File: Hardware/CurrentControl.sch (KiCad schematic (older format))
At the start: 23 parts, among them J4 Screw_Terminal_01x03, Q1 BUK7M45-40EX, U3 DAC121C081CIMK, U4 TLV172IDCK, U5 TLV172IDCK

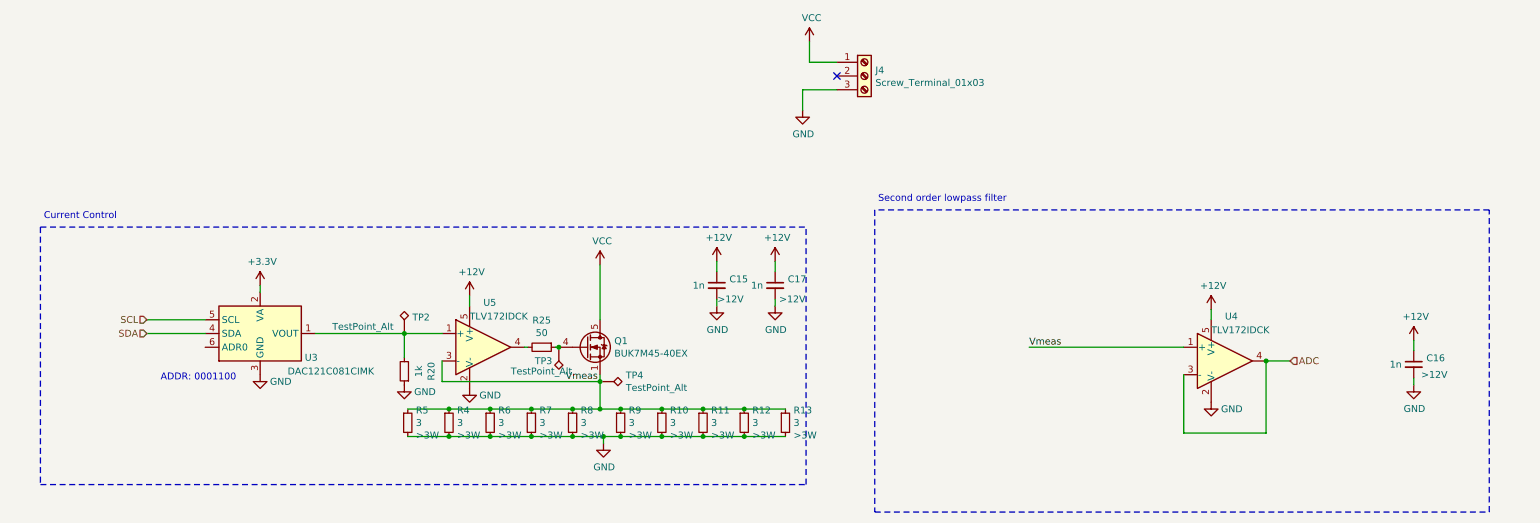
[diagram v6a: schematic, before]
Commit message: Added new FET and opamp. Repositioned parts on PCB
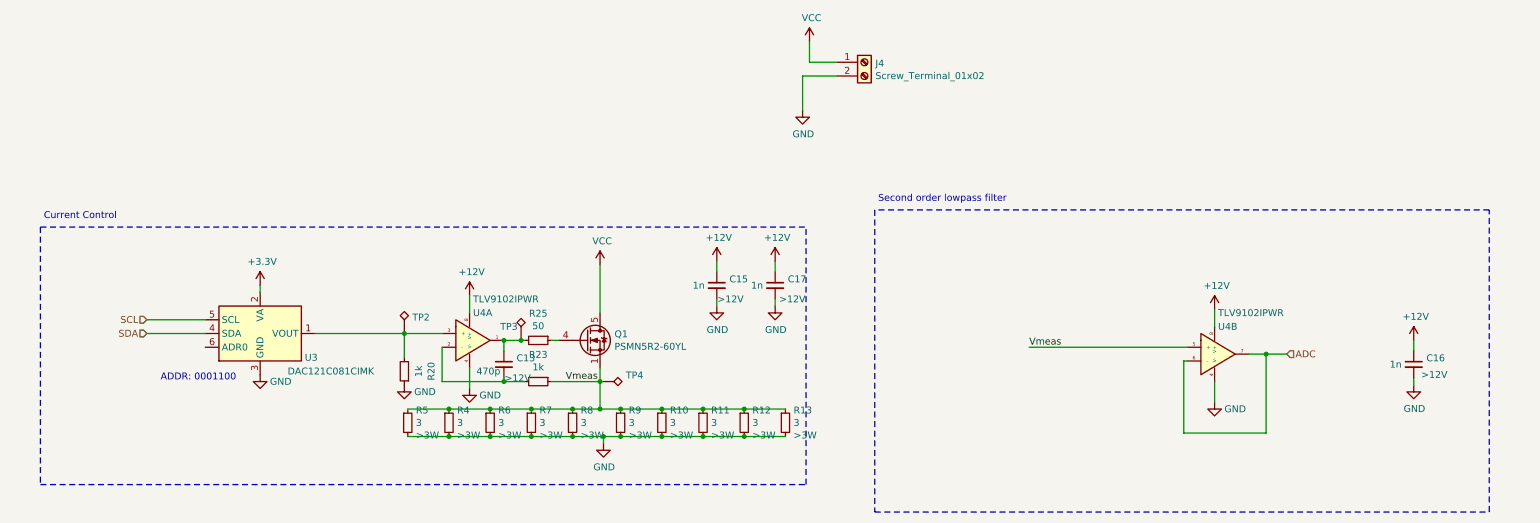
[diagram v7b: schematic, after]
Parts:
- removed J4: Screw_Terminal_01x03, Connector_TE-Connectivity:TE_826576-3_1x03_P3.96mm_Vertical, symbol Connector:Screw_Terminal_01x03
- removed Q1: BUK7M45-40EX, Package_TO_SOT_SMD:LFPAK33, symbol Transistor_FET:BUK7M45-40EX
- removed U4, U5: TLV172IDCK, Package_TO_SOT_SMD:SOT-353_SC-70-5, symbol Amplifier_Operational:TLV172IDCK
- added C13: 470p, Capacitor_SMD:C_0603_1608Metric_Pad1.05x0.95mm_HandSolder, symbol Device:C_Small
- added J4: Screw_Terminal_01x02, Connector_TE-Connectivity:TE_826576-2_1x02_P3.96mm_Vertical, symbol Connector:Screw_Terminal_01x02
- added Q1: PSMN5R2-60YL, Package_TO_SOT_SMD:LFPAK56, symbol Transistor_FET:PSMN5R2-60YL
- added R23: 1k, Resistor_SMD:R_0603_1608Metric_Pad1.05x0.95mm_HandSolder, symbol Device:R_Small
- added U4: TLV9102IPWR, Package_SO:TSSOP-8_4.4x3mm_P0.65mm, symbol E-Load-rescue:TLV9102IPWR
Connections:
- net +12V: now also U4.8 (V+), U4.8 (V+)
- net ADC: now also U4.6 (-), U4.7
- net GND: now also J4.2 (Pin_2), U4.4 (V-), U4.4 (V-)
- net VCC: now also J4.1 (Pin_1), Q1.5 (D)
- net Vmeas: now also Q1.1 (S), Q1.2 (S), Q1.3 (S), R23.1, U4.5 (+)
- net at R25.1: now also Q1.4 (G); no longer TP3.1
- net at R20.2, TP2.1, U3.1 (VOUT): now also U4.3 (+)
- net at R25.2: now also TP3.1, C13.1, U4.1
- new net: C13.2, R23.2, U4.2 (-)
- no-connect marks 1 -> 0
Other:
- moved on the sheet: R25, TP3
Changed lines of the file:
@@
 $Descr A4 11693 8268
 encoding utf-8
-Sheet 3 4
+Sheet 3 5
 Title "Electronic Load"
 Date "2020-10-12"
@@
 $EndDescr
 $Comp
-L Transistor_FET:BUK7M45-40EX Q1
-U 1 1 5F7C294E
-P 4575 3300
-F 0 "Q1" H 4779 3346 50  0000 L CNN
-F 1 "BUK7M45-40EX" H 4779 3255 50  0000 L CNN
-F 2 "Package_TO_SOT_SMD:LFPAK33" H 4775 3225 50  0001 L CIN
-F 3 "https://assets.nexperia.com/documents/data-sheet/BUK7M45-40E.pdf" V 4575 3300 50  0001 L CNN
-	1    4575 3300
-	1    0    0    -1
-$EndComp
-$Comp
 L Device:R_Small R4
 U 1 1 5F7C886E
@@
 $EndComp
 Wire Wire Line
-	4675 3500 4675 3550
+	4675 3450 4675 3550
 Connection ~ 4675 3750
 $Comp
@@
 $EndComp
 Wire Wire Line
-	4675 2700 4675 3100
+	4675 2700 4675 3050
 Connection ~ 4675 3550
 Wire Wire Line
 	4675 3550 4675 3750
-$Comp
-L Connector:Screw_Terminal_01x03 J4
-U 1 1 5F83A2FB
-P 6600 1325
-F 0 "J4" H 6680 1367 50  0000 L CNN
-F 1 "Screw_Terminal_01x03" H 6680 1276 50  0000 L CNN
-F 2 "Connector_TE-Connectivity:TE_826576-3_1x03_P3.96mm_Vertical" H 6600 1325 50  0001 C CNN
-F 3 "~" H 6600 1325 50  0001 C CNN
-	1    6600 1325
-	1    0    0    -1
-$EndComp
 $Comp
 L power:VCC #PWR0133
@@
 Wire Wire Line
 	6200 1225 6400 1225
-Wire Wire Line
-	6400 1425 6150 1425
-Wire Wire Line
-	6150 1425 6150 1575
 Wire Wire Line
 	3575 3950 3875 3950
@@
 Vmeas
 Wire Wire Line
-	8925 3500 8925 3925
-Wire Wire Line
 	8925 3925 9525 3925
 Wire Wire Line
-	9525 3925 9525 3400
+	9525 3925 9525 3350
 Text Label 7800 3300 0    50   ~ 0
 Vmeas
-Text HLabel 9700 3400 2    50   Input ~ 0
+Text HLabel 9675 3350 2    50   Input ~ 0
 ADC
 Wire Notes Line
@@
 Text Notes 625  2375 0    50   ~ 0
 Current Control
-Wire Wire Line
-	9525 3400 9700 3400
-Wire Wire Line
-	7800 3300 8925 3300
-NoConn ~ 6400 1325
-$Comp
-L Amplifier_Operational:TLV172IDCK U4
-U 1 1 5F89C6FF
-P 9125 3400
-F 0 "U4" H 9225 3725 50  0000 L CNN
-F 1 "TLV172IDCK" H 9125 3625 50  0000 L CNN
-F 2 "Package_TO_SOT_SMD:SOT-353_SC-70-5" H 9325 3400 50  0001 C CNN
-F 3 "http://www.ti.com/lit/ds/symlink/tlv172.pdf" H 9125 3400 50  0001 C CNN
-	1    9125 3400
-	1    0    0    -1
-$EndComp
-Connection ~ 9525 3400
 $Comp
 L power:GND #PWR0126
 U 1 1 5F89E085
-P 9125 3700
-F 0 "#PWR0126" H 9125 3450 50  0001 C CNN
-F 1 "GND" H 9275 3650 50  0000 C CNN
-F 2 "" H 9125 3700 50  0001 C CNN
-F 3 "" H 9125 3700 50  0001 C CNN
-	1    9125 3700
+P 9150 3700
+F 0 "#PWR0126" H 9150 3450 50  0001 C CNN
+F 1 "GND" H 9300 3650 50  0000 C CNN
+F 2 "" H 9150 3700 50  0001 C CNN
+F 3 "" H 9150 3700 50  0001 C CNN
+	1    9150 3700
 	1    0    0    -1
 $EndComp
@@
 L power:+12V #PWR0139
 U 1 1 5F89EB39
-P 9125 3025
-F 0 "#PWR0139" H 9125 2875 50  0001 C CNN
-F 1 "+12V" H 9140 3198 50  0000 C CNN
-F 2 "" H 9125 3025 50  0001 C CNN
-F 3 "" H 9125 3025 50  0001 C CNN
-	1    9125 3025
-	1    0    0    -1
-$EndComp
-Wire Wire Line
-	9125 3025 9125 3100
+P 9150 3025
+F 0 "#PWR0139" H 9150 2875 50  0001 C CNN
+F 1 "+12V" H 9165 3198 50  0000 C CNN
+F 2 "" H 9150 3025 50  0001 C CNN
+F 3 "" H 9150 3025 50  0001 C CNN
+	1    9150 3025
+	1    0    0    -1
+$EndComp
 $Comp
 L power:+12V #PWR03
@@
 $EndComp
 $Comp
-L Amplifier_Operational:TLV172IDCK U5
-U 1 1 5F8E48FD
-P 3725 3300
-F 0 "U5" H 3825 3625 50  0000 L CNN
-F 1 "TLV172IDCK" H 3725 3525 50  0000 L CNN
-F 2 "Package_TO_SOT_SMD:SOT-353_SC-70-5" H 3925 3300 50  0001 C CNN
-F 3 "http://www.ti.com/lit/ds/symlink/tlv172.pdf" H 3725 3300 50  0001 C CNN
-	1    3725 3300
-	1    0    0    -1
-$EndComp
-$Comp
 L Device:R_Small R25
 U 1 1 5F8EC11D
-P 4250 3300
-F 0 "R25" V 4054 3300 50  0000 C CNN
-F 1 "50" V 4145 3300 50  0000 C CNN
-F 2 "Resistor_SMD:R_0603_1608Metric_Pad1.05x0.95mm_HandSolder" H 4250 3300 50  0001 C CNN
-F 3 "~" H 4250 3300 50  0001 C CNN
-	1    4250 3300
+P 4225 3250
+F 0 "R25" V 4029 3250 50  0000 C CNN
+F 1 "50" V 4120 3250 50  0000 C CNN
+F 2 "Resistor_SMD:R_0603_1608Metric_Pad1.05x0.95mm_HandSolder" H 4225 3250 50  0001 C CNN
+F 3 "~" H 4225 3250 50  0001 C CNN
+	1    4225 3250
 	0    1    1    0
 $EndComp
 Wire Wire Line
-	4150 3300 4125 3300
-Wire Wire Line
-	4350 3300 4375 3300
-Wire Wire Line
-	3525 3400 3525 3550
-Wire Wire Line
-	3525 3550 4675 3550
+	4325 3250 4375 3250
+Wire Wire Line
+	3525 3550 3975 3550
 $Comp
 L power:+12V #PWR07
@@
 	1    0    0    -1
 $EndComp
-Wire Wire Line
-	3725 2925 3725 3000
 $Comp
 L power:GND #PWR08
@@
 P 3250 3200
 F 0 "TP2" H 3308 3318 50  0000 L CNN
-F 1 "TestPoint_Alt" H 2725 3250 50  0000 L CNN
+F 1 "TestPoint_Alt" H 2725 3250 50  0001 L CNN
 F 2 "TestPoint:TestPoint_Keystone_5000-5004_Miniature" H 3450 3200 50  0001 C CNN
 F 3 "~" H 3450 3200 50  0001 C CNN
@@
 P 4675 3550
 F 0 "TP4" V 4629 3738 50  0000 L CNN
-F 1 "TestPoint_Alt" V 4720 3738 50  0000 L CNN
+F 1 "TestPoint_Alt" V 4720 3738 50  0001 L CNN
 F 2 "TestPoint:TestPoint_Keystone_5000-5004_Miniature" H 4875 3550 50  0001 C CNN
 F 3 "~" H 4875 3550 50  0001 C CNN
@@
 L Connector:TestPoint_Alt TP3
 U 1 1 5F925FD4
-P 4375 3300
-F 0 "TP3" H 4550 3400 50  0000 R CNN
-F 1 "TestPoint_Alt" H 4725 3475 50  0000 R CNN
-F 2 "TestPoint:TestPoint_Keystone_5000-5004_Miniature" H 4575 3300 50  0001 C CNN
-F 3 "~" H 4575 3300 50  0001 C CNN
-	1    4375 3300
-	-1   0    0    1
-$EndComp
-Connection ~ 4375 3300
+P 4100 3250
+F 0 "TP3" H 4075 3350 50  0000 R CNN
+F 1 "TestPoint_Alt" V 4100 4000 50  0001 R CNN
+F 2 "TestPoint:TestPoint_Keystone_5000-5004_Miniature" H 4300 3250 50  0001 C CNN
+F 3 "~" H 4300 3250 50  0001 C CNN
+	1    4100 3250
+	1    0    0    -1
+$EndComp
 $Comp
 L Analog_DAC:DAC121C081CIMK U3
@@
 	1    0    0    -1
 $EndComp
-Wire Wire Line
-	1800 3100 1375 3100
-Wire Wire Line
-	1800 3200 1375 3200
 Text HLabel 1375 3100 0    50   Input ~ 0
 SCL
@@
 	1    0    0    -1
 $EndComp
+$Comp
+L E-Load-rescue:TLV9102IPWR U4
+U 1 1 5F9CD8CF
+P 3825 3250
+F 0 "U4" H 3750 3450 50  0000 L CNN
+F 1 "TLV9102IPWR" H 3750 3550 50  0000 L CNN
+F 2 "Package_SO:TSSOP-8_4.4x3mm_P0.65mm" H 3825 3250 50  0001 C CNN
+F 3 "" H 3825 3250 50  0001 C CNN
+	1    3825 3250
+	1    0    0    -1
+$EndComp
+Wire Wire Line
+	3975 3250 4100 3250
+Wire Wire Line
+	3725 2925 3725 3050
+Wire Wire Line
+	3725 3450 3725 3600
+Wire Wire Line
+	3525 3300 3525 3550
+$Comp
+L E-Load-rescue:TLV9102IPWR U4
+U 2 1 5F9D991A
+P 9250 3350
+F 0 "U4" H 9175 3550 50  0000 L CNN
+F 1 "TLV9102IPWR" H 9175 3650 50  0000 L CNN
+F 2 "Package_SO:TSSOP-8_4.4x3mm_P0.65mm" H 9250 3350 50  0001 C CNN
+F 3 "" H 9250 3350 50  0001 C CNN
+	2    9250 3350
+	1    0    0    -1
+$EndComp
+Wire Wire Line
+	9150 3025 9150 3150
+Wire Wire Line
+	9150 3550 9150 3700
+Wire Wire Line
+	7800 3300 8950 3300
+Wire Wire Line
+	9400 3350 9525 3350
+Connection ~ 9525 3350
+Wire Wire Line
+	9525 3350 9675 3350
+Wire Wire Line
+	8950 3400 8925 3400
+Wire Wire Line
+	8925 3400 8925 3925
+$Comp
+L Device:R_Small R23
+U 1 1 5F9E4082
+P 4225 3550
+F 0 "R23" V 4029 3550 50  0000 C CNN
+F 1 "1k" V 4120 3550 50  0000 C CNN
+F 2 "Resistor_SMD:R_0603_1608Metric_Pad1.05x0.95mm_HandSolder" H 4225 3550 50  0001 C CNN
+F 3 "~" H 4225 3550 50  0001 C CNN
+	1    4225 3550
+	0    1    1    0
+$EndComp
+Wire Wire Line
+	4325 3550 4675 3550
+$Comp
+L Device:C_Small C13
+U 1 1 5F9E4F80
+P 3975 3425
+F 0 "C13" H 4067 3471 50  0000 L CNN
+F 1 "470p" H 3775 3375 50  0000 L CNN
+F 2 "Capacitor_SMD:C_0603_1608Metric_Pad1.05x0.95mm_HandSolder" H 3975 3425 50  0001 C CNN
+F 3 "~" H 3975 3425 50  0001 C CNN
+F 4 ">12V" H 4075 3325 50  0000 C CNN "Voltage"
+	1    3975 3425
+	1    0    0    -1
+$EndComp
+Wire Wire Line
+	3975 3325 3975 3250
+Connection ~ 3975 3250
+Wire Wire Line
+	3975 3525 3975 3550
+Connection ~ 3975 3550
+Wire Wire Line
+	3975 3550 4125 3550
+$Comp
+L Transistor_FET:PSMN5R2-60YL Q1
+U 1 1 5F9E861A
+P 4575 3250
+F 0 "Q1" H 4780 3296 50  0000 L CNN
+F 1 "PSMN5R2-60YL" H 4780 3205 50  0000 L CNN
+F 2 "Package_TO_SOT_SMD:LFPAK56" H 4725 3250 50  0001 C CNN
+F 3 "https://assets.nexperia.com/documents/data-sheet/PSMN5R2-60YL.pdf" H 4575 3250 50  0001 C CNN
+	1    4575 3250
+	1    0    0    -1
+$EndComp
+Connection ~ 4100 3250
+Wire Wire Line
+	4100 3250 4125 3250
+Wire Wire Line
+	1375 3100 1800 3100
+Wire Wire Line
+	1375 3200 1800 3200
+$Comp
+L Connector:Screw_Terminal_01x02 J4
+U 1 1 5FA56BB5
+P 6600 1225
+F 0 "J4" H 6680 1217 50  0000 L CNN
+F 1 "Screw_Terminal_01x02" H 6680 1126 50  0000 L CNN
+F 2 "Connector_TE-Connectivity:TE_826576-2_1x02_P3.96mm_Vertical" H 6600 1225 50  0001 C CNN
+F 3 "~" H 6600 1225 50  0001 C CNN
+	1    6600 1225
+	1    0    0    -1
+$EndComp
+Wire Wire Line
+	6150 1325 6400 1325
+Wire Wire Line
+	6150 1325 6150 1575
 $EndSCHEMATC
